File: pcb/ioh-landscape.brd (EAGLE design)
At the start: 80 x 41.9 mm, 35 parts

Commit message: place new bsides logo
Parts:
- U$2: value BSIDES -> (none)
- moved U$2 1.62 mm to (2.48, 29.6)
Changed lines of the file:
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@@
 <element name="JP3" library="SparkFun-Connectors" package="FTDI_DEVICE_SIDE" value="FTDI_DEVICE" x="13.97" y="39.37" rot="R180"/>
 <element name="JP4" library="SparkFun-Connectors" package="1X03_LOCK" value="" x="20.32" y="35.56" rot="R180"/>
-<element name="U$2" library="ioh-1" package="BSIDES" value="BSIDES" x="2.54" y="27.94"/>
+<element name="U$2" library="ioh-1" package="BSIDES" value="" x="2.484775" y="29.558325"/>
 </elements>
 <signals>

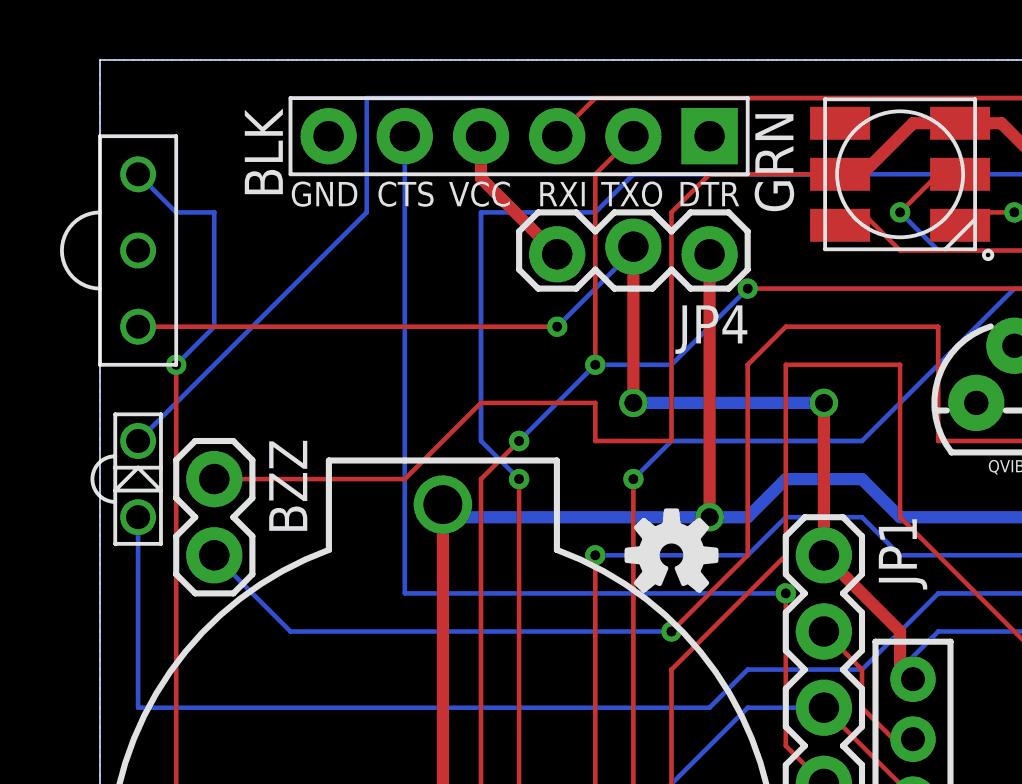
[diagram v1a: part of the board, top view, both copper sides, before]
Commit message: switch from cts->spimiso to dtr->spimiso
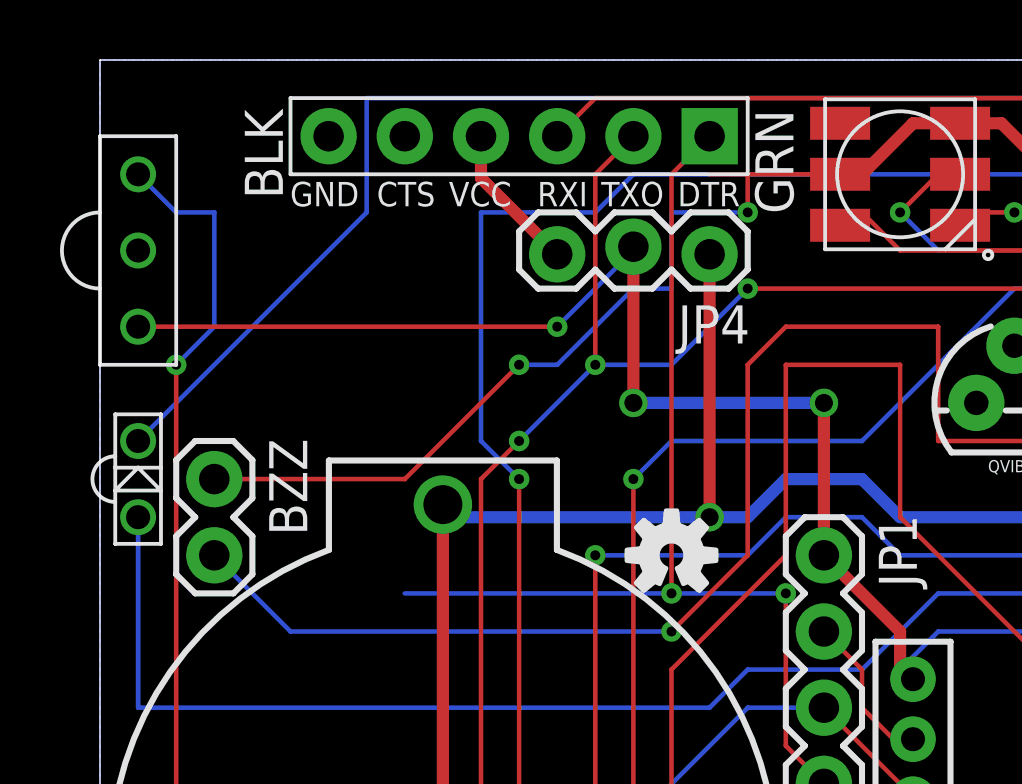
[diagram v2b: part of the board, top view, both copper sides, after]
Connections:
- net GND: now also JP3.P$5
- net SPIMISO: now also JP3.P$1; no longer JP3.P$5
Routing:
- net VCC: track 127.4 -> 124.6 mm, vias 1 -> 3
- net SPIMISO: track 38.8 -> 39.4 mm, vias 1 -> 2
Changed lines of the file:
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@@
 <contactref element="JP1" pad="4"/>
 <contactref element="U$1" pad="4"/>
-<contactref element="JP3" pad="P$5"/>
 <wire x1="24.13" y1="17.78" x2="26.67" y2="15.24" width="0.1524" layer="1"/>
 <wire x1="26.67" y1="15.24" x2="27.1" y2="15.27" width="0.1524" layer="1"/>
-<wire x1="10.16" y1="24.13" x2="10.16" y2="39.37" width="0.1524" layer="16"/>
-<wire x1="22.86" y1="24.13" x2="10.16" y2="24.13" width="0.1524" layer="16"/>
+<wire x1="22.86" y1="24.13" x2="19.05" y2="24.13" width="0.1524" layer="16"/>
+<wire x1="19.05" y1="24.13" x2="10.16" y2="24.13" width="0.1524" layer="16"/>
 <wire x1="22.86" y1="19.05" x2="22.86" y2="24.13" width="0.1524" layer="1"/>
 <wire x1="24.13" y1="17.78" x2="22.86" y2="19.05" width="0.1524" layer="1"/>
 <via x="22.86" y="24.13" extent="1-16" drill="0.3302"/>
+<contactref element="JP3" pad="P$1"/>
+<wire x1="19.05" y1="38.1" x2="20.32" y2="39.37" width="0.1524" layer="1"/>
+<wire x1="19.05" y1="24.13" x2="19.05" y2="38.1" width="0.1524" layer="1"/>
+<via x="19.05" y="24.13" extent="1-16" drill="0.3302"/>
 </signal>
 <signal name="N$8">
@@
 <wire x1="35.56" y1="31.75" x2="31.75" y2="35.56" width="0.1524" layer="1"/>
 <wire x1="35.56" y1="30.48" x2="35.56" y2="31.75" width="0.1524" layer="1"/>
-<wire x1="78.74" y1="35.56" x2="73.5584" y2="30.5308" width="0" layer="19" extent="1-1"/>
+<contactref element="JP3" pad="P$5"/>
+<wire x1="1.27" y1="35.56" x2="1.26998125" y2="35.559965625" width="0.1524" layer="16"/>
+<wire x1="7.62" y1="39.37" x2="10.16" y2="39.37" width="0" layer="19" extent="1-1"/>
 <wire x1="1.27" y1="35.56" x2="7.62" y2="39.37" width="0" layer="19" extent="1-1"/>
 <wire x1="27.1" y1="3.27" x2="29.21" y2="30.48" width="0" layer="19" extent="1-1"/>
@@
 <wire x1="25.4" y1="38.1" x2="24.67" y2="38.1" width="0.1524" layer="1"/>
 <wire x1="31.75" y1="38.1" x2="32.29" y2="38.1" width="0.1524" layer="1"/>
-<wire x1="10.16" y1="27.94" x2="3.81" y2="27.94" width="0.1524" layer="1"/>
-<wire x1="12.7" y1="30.48" x2="10.16" y2="27.94" width="0.1524" layer="1"/>
-<wire x1="16.51" y1="30.48" x2="12.7" y2="30.48" width="0.1524" layer="1"/>
-<wire x1="16.51" y1="29.21" x2="16.51" y2="30.48" width="0.1524" layer="1"/>
-<wire x1="19.05" y1="29.21" x2="16.51" y2="29.21" width="0.1524" layer="1"/>
-<wire x1="19.05" y1="36.83" x2="19.05" y2="29.21" width="0.1524" layer="1"/>
-<wire x1="20.32" y1="38.1" x2="19.05" y2="36.83" width="0.1524" layer="1"/>
-<wire x1="24.67" y1="38.1" x2="20.32" y2="38.1" width="0.1524" layer="1"/>
+<wire x1="24.67" y1="38.1" x2="21.59" y2="38.1" width="0.1524" layer="1"/>
+<wire x1="21.59" y1="38.1" x2="20.32" y2="38.1" width="0.1524" layer="1"/>
 <wire x1="40.64" y1="38.1" x2="39.91" y2="38.1" width="0.1524" layer="1"/>
 <wire x1="46.99" y1="38.1" x2="47.53" y2="38.1" width="0.1524" layer="1"/>
@@
 <wire x1="35.56" y1="39.37" x2="34.29" y2="38.1" width="0.1524" layer="1"/>
 <wire x1="35.56" y1="39.37" x2="36.29" y2="39.8" width="0.1524" layer="1"/>
+<wire x1="10.16" y1="27.94" x2="3.81" y2="27.94" width="0.1524" layer="1"/>
+<wire x1="13.97" y1="31.75" x2="10.16" y2="27.94" width="0.1524" layer="1"/>
+<wire x1="15.24" y1="31.75" x2="13.97" y2="31.75" width="0.1524" layer="16"/>
+<wire x1="17.78" y1="34.29" x2="15.24" y2="31.75" width="0.1524" layer="16"/>
+<wire x1="19.05" y1="34.29" x2="17.78" y2="34.29" width="0.1524" layer="16"/>
+<wire x1="19.05" y1="36.83" x2="19.05" y2="34.29" width="0.1524" layer="16"/>
+<wire x1="21.59" y1="36.83" x2="19.05" y2="36.83" width="0.1524" layer="16"/>
+<wire x1="21.59" y1="38.1" x2="21.59" y2="36.83" width="0.1524" layer="1"/>
+<via x="13.97" y="31.75" extent="1-16" drill="0.3302"/>
+<via x="21.59" y="36.83" extent="1-16" drill="0.3302"/>
 </signal>
 <signal name="N$1">

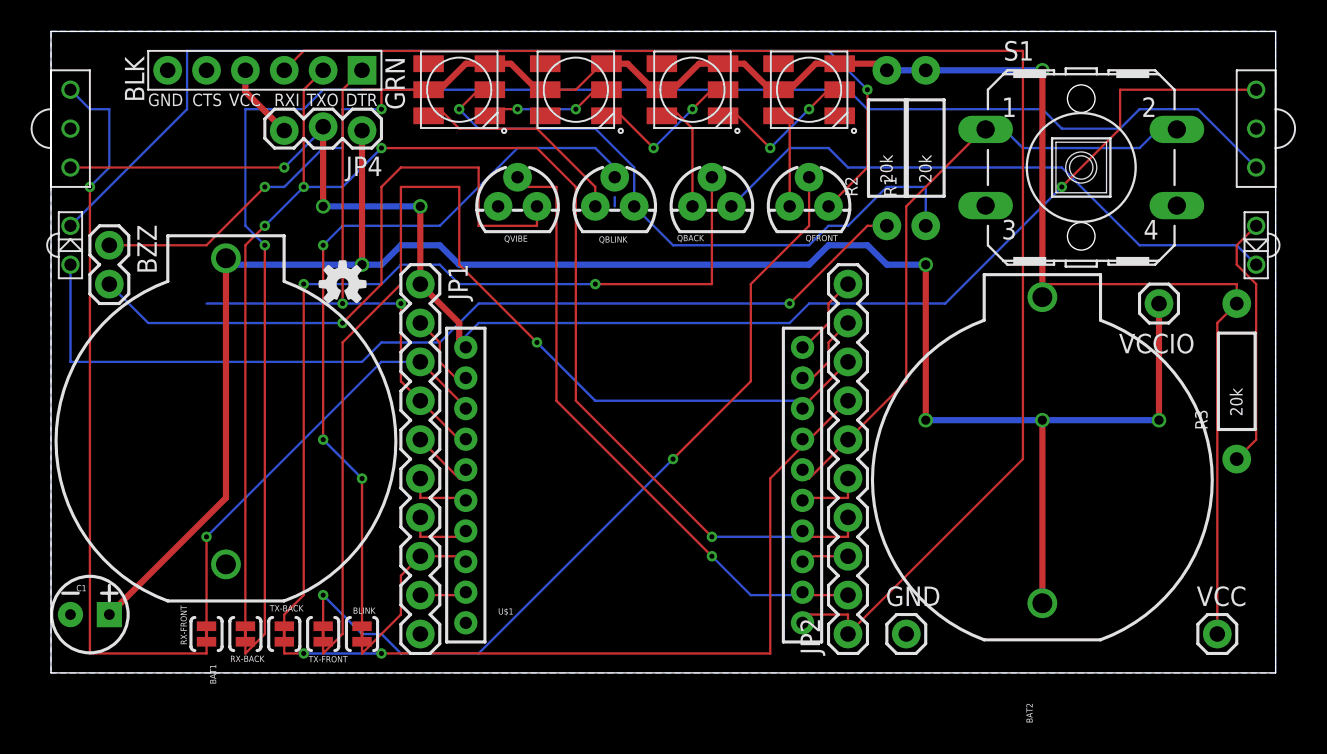
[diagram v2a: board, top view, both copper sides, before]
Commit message: added top ground plane and several ground vias. adjusted a few traces to pass drc. added cam file for generating gerbers, plus generated gerbers. added top/bottom preview images from gerbv.
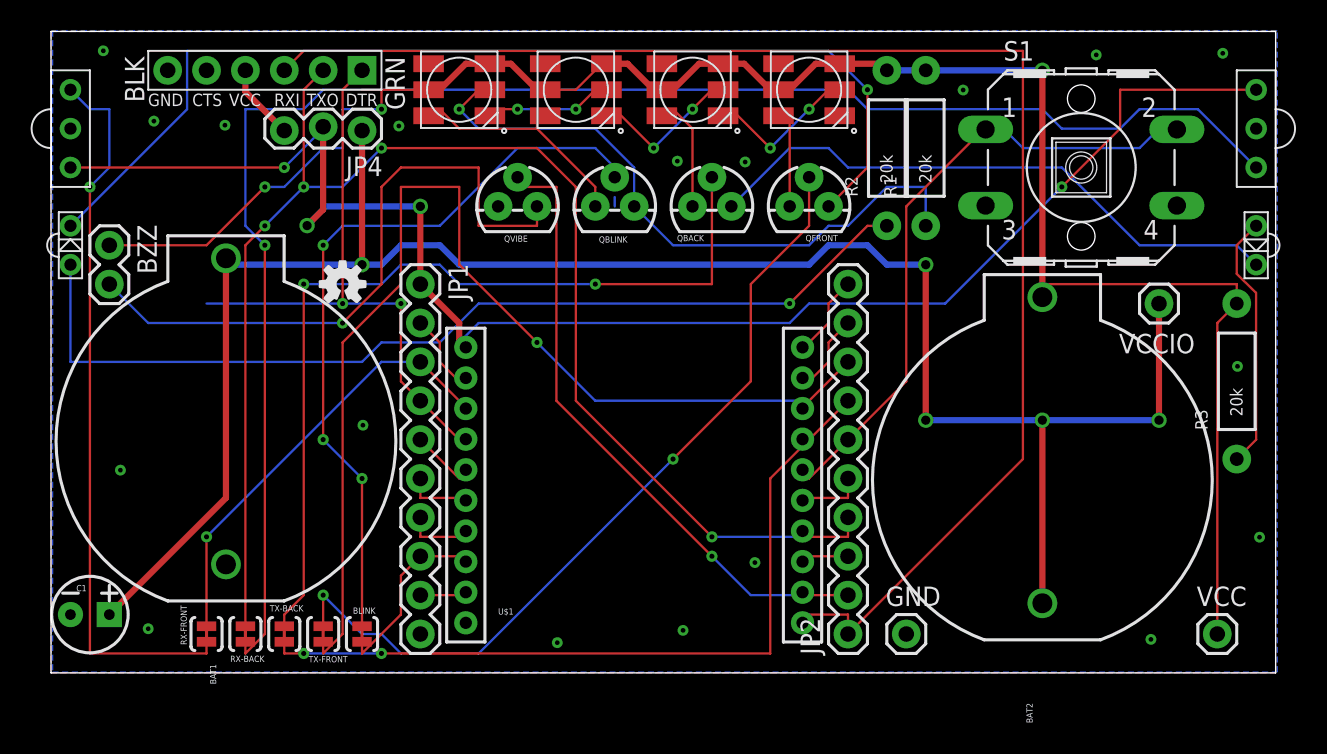
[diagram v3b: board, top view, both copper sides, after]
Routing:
- net VCCIO: track 100.6 -> 103.6 mm
- net GND: vias 0 -> 18
- added copper zone on layer 1, net GND
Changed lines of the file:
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@@
 </class>
 </classes>
-<designrules name="LaenPCBOrder">
-<description language="de">&lt;b&gt;EAGLE Design Rules&lt;/b&gt;
+<designrules name="DFRobot_Eagle_Rule_v0.4">
+<description language="en">
+&lt;b&gt;EAGLE Design Rules&lt;/b&gt;
 &lt;p&gt;
-Die Standard-Design-Rules sind so gewählt, dass sie für
-die meisten Anwendungen passen. Sollte ihre Platine
-besondere Anforderungen haben, treffen Sie die erforderlichen
-Einstellungen hier und speichern die Design Rules unter
-einem neuen Namen ab.</description>
-<description language="en">&lt;b&gt;Laen's PCB Order Design Rules&lt;/b&gt;
+The default Design Rules have been set to cover
+a wide range of applications. Your particular design
+may have different requirements, so please make the
+necessary adjustments and save your customized
+design rules under a new name.
+</description>
+<description language="it">
+&lt;b&gt;EAGLE Design Rules&lt;/b&gt;
 &lt;p&gt;
-Please make sure your boards conform to these design rules.</description>
+The default Design Rules have been set to cover
+a wide range of applications. Your particular design
+may have different requirements, so please make the
+necessary adjustments and save your customized
+design rules under a new name.</description>
 <param name="layerSetup" value="(1*16)"/>
-<param name="mtCopper" value="0.0356mm 0.0356mm 0.0356mm 0.0356mm 0.0356mm 0.0356mm 0.0356mm 0.0356mm 0.0356mm 0.0356mm 0.0356mm 0.0356mm 0.0356mm 0.0356mm 0.0356mm 0.0356mm"/>
-<param name="mtIsolate" value="1.5011mm 0.1499mm 0.2007mm 0.1499mm 0.2007mm 0.1499mm 0.2007mm 0.1499mm 0.2007mm 0.1499mm 0.2007mm 0.1499mm 0.2007mm 0.1499mm 0.2007mm"/>
+<param name="mtCopper" value="0.035mm 0.035mm 0.035mm 0.035mm 0.035mm 0.035mm 0.035mm 0.035mm 0.035mm 0.035mm 0.035mm 0.035mm 0.035mm 0.035mm 0.035mm 0.035mm"/>
+<param name="mtIsolate" value="1.5mm 0.15mm 0.2mm 0.15mm 0.2mm 0.15mm 0.2mm 0.15mm 0.2mm 0.15mm 0.2mm 0.15mm 0.2mm 0.15mm 0.2mm"/>
 <param name="mdWireWire" value="6mil"/>
 <param name="mdWirePad" value="6mil"/>
@@
 <param name="mdPadVia" value="6mil"/>
 <param name="mdViaVia" value="6mil"/>
-<param name="mdSmdPad" value="6mil"/>
-<param name="mdSmdVia" value="6mil"/>
-<param name="mdSmdSmd" value="6mil"/>
+<param name="mdSmdPad" value="0mil"/>
+<param name="mdSmdVia" value="0mil"/>
+<param name="mdSmdSmd" value="0mil"/>
 <param name="mdViaViaSameLayer" value="8mil"/>
 <param name="mnLayersViaInSmd" value="2"/>
-<param name="mdCopperDimension" value="15mil"/>
-<param name="mdDrill" value="6mil"/>
+<param name="mdCopperDimension" value="10mil"/>
+<param name="mdDrill" value="10mil"/>
 <param name="mdSmdStop" value="0mil"/>
 <param name="msWidth" value="6mil"/>
-<param name="msDrill" value="13mil"/>
-<param name="msMicroVia" value="13mil"/>
+<param name="msDrill" value="12mil"/>
+<param name="msMicroVia" value="12mil"/>
 <param name="msBlindViaRatio" value="0.5"/>
 <param name="rvPadTop" value="0.25"/>
@@
 <param name="rvMicroViaOuter" value="0.25"/>
 <param name="rvMicroViaInner" value="0.25"/>
-<param name="rlMinPadTop" value="7mil"/>
+<param name="rlMinPadTop" value="12mil"/>
 <param name="rlMaxPadTop" value="20mil"/>
-<param name="rlMinPadInner" value="7mil"/>
+<param name="rlMinPadInner" value="10mil"/>
 <param name="rlMaxPadInner" value="20mil"/>
-<param name="rlMinPadBottom" value="7mil"/>
+<param name="rlMinPadBottom" value="12mil"/>
 <param name="rlMaxPadBottom" value="20mil"/>
-<param name="rlMinViaOuter" value="7mil"/>
+<param name="rlMinViaOuter" value="8mil"/>
 <param name="rlMaxViaOuter" value="20mil"/>
-<param name="rlMinViaInner" value="7mil"/>
+<param name="rlMinViaInner" value="8mil"/>
 <param name="rlMaxViaInner" value="20mil"/>
 <param name="rlMinMicroViaOuter" value="4mil"/>
@@
 <param name="mvStopFrame" value="1"/>
 <param name="mvCreamFrame" value="0"/>
-<param name="mlMinStopFrame" value="3mil"/>
-<param name="mlMaxStopFrame" value="3mil"/>
+<param name="mlMinStopFrame" value="2mil"/>
+<param name="mlMaxStopFrame" value="2mil"/>
 <param name="mlMinCreamFrame" value="0mil"/>
 <param name="mlMaxCreamFrame" value="0mil"/>
-<param name="mlViaStopLimit" value="0mil"/>
+<param name="mlViaStopLimit" value="25mil"/>
 <param name="srRoundness" value="0"/>
 <param name="srMinRoundness" value="0mil"/>
@@
 <contactref element="JP3" pad="P$5"/>
 <wire x1="1.27" y1="35.56" x2="1.26998125" y2="35.559965625" width="0.1524" layer="16"/>
-<wire x1="7.62" y1="39.37" x2="10.16" y2="39.37" width="0" layer="19" extent="1-1"/>
-<wire x1="1.27" y1="35.56" x2="7.62" y2="39.37" width="0" layer="19" extent="1-1"/>
-<wire x1="27.1" y1="3.27" x2="29.21" y2="30.48" width="0" layer="19" extent="1-1"/>
+<via x="4.534784375" y="13.24535625" extent="1-16" drill="0.305815625"/>
+<via x="6.348696875" y="2.88406875" extent="1-16" drill="0.305815625"/>
+<via x="33.07724375" y="1.976121875" extent="1-16" drill="0.305815625"/>
+<via x="41.29320625" y="2.777253125" extent="1-16" drill="0.305815625"/>
+<via x="45.988040625" y="7.210175" extent="1-16" drill="0.305815625"/>
+<via x="71.86298125" y="2.18975625" extent="1-16" drill="0.305815625"/>
+<via x="78.958584375" y="8.86584375" extent="1-16" drill="0.305815625"/>
+<via x="76.557815625" y="40.483790625" extent="1-16" drill="0.305815625"/>
+<via x="68.28850625" y="40.376975" extent="1-16" drill="0.305815625"/>
+<via x="59.592390625" y="38.0804" extent="1-16" drill="0.305815625"/>
+<via x="45.3478375" y="33.3804375" extent="1-16" drill="0.305815625"/>
+<via x="40.919753125" y="33.43384375" extent="1-16" drill="0.305815625"/>
+<via x="22.72726875" y="35.73041875" extent="1-16" drill="0.305815625"/>
+<via x="11.363634375" y="35.783828125" extent="1-16" drill="0.305815625"/>
+<via x="6.72215" y="36.050871875" extent="1-16" drill="0.305815625"/>
+<via x="3.414428125" y="40.644021875" extent="1-16" drill="0.305815625"/>
+<polygon width="0.4064" layer="1">
+<vertex x="0" y="41.91"/>
+<vertex x="0" y="0"/>
+<vertex x="80.01" y="0"/>
+<vertex x="80.01" y="41.91"/>
+</polygon>
+<via x="20.379853125" y="16.182834375" extent="1-16" drill="0.305815625"/>
+<via x="77.518125" y="20.028259375" extent="1-16" drill="0.305815625"/>
 </signal>
 <signal name="VCCIO">
@@
 <wire x1="24.13" y1="25.4" x2="24.13" y2="30.48" width="0.4064" layer="1"/>
 <via x="24.13" y="30.48" extent="1-16" drill="0.6" shape="square"/>
-<wire x1="24.13" y1="30.48" x2="17.78" y2="30.48" width="0.4064" layer="16"/>
-<via x="17.78" y="30.48" extent="1-16" drill="0.6" shape="square"/>
-<wire x1="17.78" y1="35.687" x2="17.78" y2="30.48" width="0.4064" layer="1"/>
+<via x="16.730721875" y="29.22498125" extent="1-16" drill="0.6" shape="square"/>
 <wire x1="24.13" y1="25.4" x2="26.67" y2="22.86" width="0.4064" layer="1"/>
 <wire x1="26.67" y1="22.86" x2="26.67" y2="21.7" width="0.4064" layer="1"/>
@@
 <via x="15.24" y="33.02" extent="1-16" drill="0.3302"/>
 <via x="66.04" y="31.75" extent="1-16" drill="0.3302"/>
+<wire x1="17.78" y1="30.274259375" x2="16.730721875" y2="29.22498125" width="0.4064" layer="16"/>
+<wire x1="17.985740625" y1="30.48" x2="24.13" y2="30.48" width="0.4064" layer="16"/>
+<wire x1="16.730721875" y1="29.22498125" x2="17.78" y2="30.274259375" width="0.4064" layer="1"/>
+<wire x1="17.78" y1="30.274259375" x2="17.78" y2="35.687" width="0.4064" layer="1"/>
+<wire x1="17.78" y1="30.274259375" x2="17.985740625" y2="30.48" width="0" layer="19" extent="16-16"/>
 </signal>
 <signal name="VCC">
@@
 <contactref element="IRBACK" pad="A"/>
 <wire x1="77.47" y1="27.94" x2="78.74" y2="29.21" width="0.1524" layer="1"/>
-<wire x1="77.47" y1="26.67" x2="77.47" y2="27.94" width="0.1524" layer="1"/>
-<wire x1="78.74" y1="25.4" x2="77.47" y2="26.67" width="0.1524" layer="1"/>
-<wire x1="78.74" y1="15.24" x2="78.74" y2="25.4" width="0.1524" layer="1"/>
+<wire x1="77.47" y1="26.066546875" x2="77.47" y2="27.94" width="0.1524" layer="1"/>
+<wire x1="78.73138125" y1="24.83103125" x2="77.47" y2="26.066546875" width="0.1524" layer="1"/>
+<wire x1="78.74" y1="15.24" x2="78.73138125" y2="24.83103125" width="0.1524" layer="1"/>
 <wire x1="77.47" y1="13.97" x2="78.74" y2="15.24" width="0.1524" layer="1"/>
 </signal>
@@
 </signal>
 <signal name="N$7">
+<wire x1="36.83" y1="30.48" x2="36.83" y2="31.0896" width="0.1524" layer="16"/>
 <polygon width="0.4064" layer="16">
-<vertex x="0" y="41.91"/>
-<vertex x="0" y="0"/>
-<vertex x="80.01" y="0"/>
-<vertex x="80.01" y="41.91"/>
+<vertex x="0.1067" y="41.963409375"/>
+<vertex x="0.1067" y="0.053409375"/>
+<vertex x="80.1167" y="0.053409375"/>
+<vertex x="80.1167" y="41.963409375"/>
 </polygon>
-<wire x1="36.83" y1="30.48" x2="36.83" y2="31.0896" width="0.1524" layer="16"/>
 </signal>
 </signals>
